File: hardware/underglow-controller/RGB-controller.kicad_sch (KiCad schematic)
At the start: 0 parts

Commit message: iasdf
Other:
- removed sheet Motor-Control
- removed sheet Pico Remote Proc
- note removed: "SPID = MOSI = RPRX SPIQ = MISO = RPTX"

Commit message: schematic rework progress
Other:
- sheet Connectors ports: added CAN_H, CAN_L, DI_1, DI_2, DI_3, DI_4, IGNITION_IN, PIXEL_1, PIXEL_2, RGB1_12V, RGB1_B, RGB1_G, RGB1_R, RGB2_12V, RGB2_B, RGB2_G, RGB2_R, USB_D_N, USB_D_P, USB_GND, USB_VBUS, VBAT; removed CAN_N, CAN_P, CONN_ESP_USB_D_N, CONN_ESP_USB_D_P, CONN_RP_USB_D_N, CONN_RP_USB_D_P, FUSE_OUT, GPI1, GPI2, GPI3, GPI4, GPO1, GPO2, GPO3, LEDA_OUT, MOTOR1_OUT1, MOTOR1_OUT2, MOTOR2_OUT1, MOTOR2_OUT2, VIN, VOUT
- sheet External-IO ports: added CSN, GP05, GP06, GPIO_GP05, GPIO_GP06, GPO4, IGNITION, LED1_IN, LED1_OUT, LED2_IN, LED2_OUT, LHI, MISO, MOSI, PWMI1, PWMI2, RGB1_12V, SCLK, VBATT, VIN; removed LEDA_IN, LEDA_OUT, VOUT_EN

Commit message: schematic almost done
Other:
- sheet SX1276 renamed SX1231
- sheet Connectors ports: added IGNITION, VBATT; removed IGNITION_IN, VBAT
- sheet ESP32-S3 ports: added DI_1, DI_2, DI_3, DI_4, LHI, PIXEL1_OUT, PIXEL2_OUT, RGB1_B, RGB1_G, RGB1_PWM, RGB1_R, RGB2_B, RGB2_G, RGB2_PWM, RGB2_R; removed FSPICS2, MCPWM0_ENA, MCPWM0_ENB, MCPWM0_INA, MCPWM0_INB, MCPWM1_ENA, MCPWM1_ENB, MCPWM1_INA, MCPWM1_INB, MCPWM_FAULT, MCPWM_RESET, MCPWM_SLEEP, RP2040_EN
- sheet External-IO ports: added DI_1, DI_2, DI_3, DI_4, PIXEL1_IN, PIXEL1_OUT, PIXEL2_IN, PIXEL2_OUT, RGB1_B, RGB1_G, RGB1_R, RGB2_12V, RGB2_B, RGB2_G, RGB2_R, TTL_DI_1, TTL_DI_2, TTL_DI_3, TTL_DI_4, TTL_RGB1_B, TTL_RGB1_G, TTL_RGB1_R, TTL_RGB2_B, TTL_RGB2_G, TTL_RGB2_R; removed GP01, GP02, GP03, GP05, GP06, GPI1, GPI2, GPI3, GPI4, GPIO_GP01, GPIO_GP02, GPIO_GP03, GPIO_GP04, GPIO_GP05, GPIO_GP06, GPIO_GPI1, GPIO_GPI2, GPIO_GPI3, GPIO_GPI4, GPO4, LED1_IN, LED1_OUT, LED2_IN, LED2_OUT
- sheet Power ports: added IGNITION, VBATT; removed VBAT, VIN, VOUT, VOUT_EN
- sheet SX1231: file SX1276.kicad_sch -> SX1231.kicad_sch

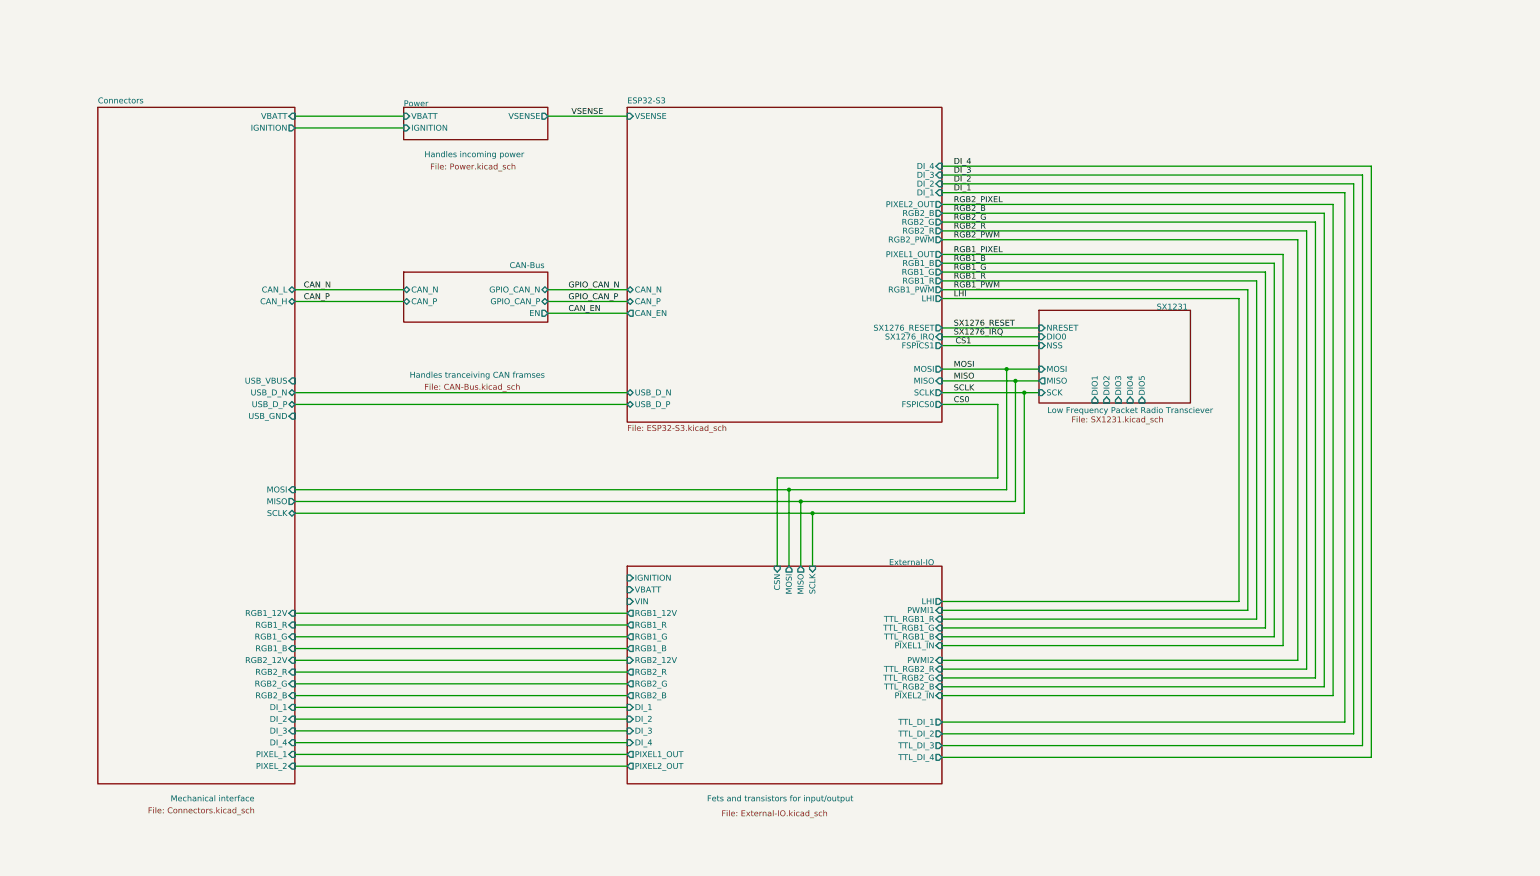
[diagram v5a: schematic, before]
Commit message: fix main sheet grid
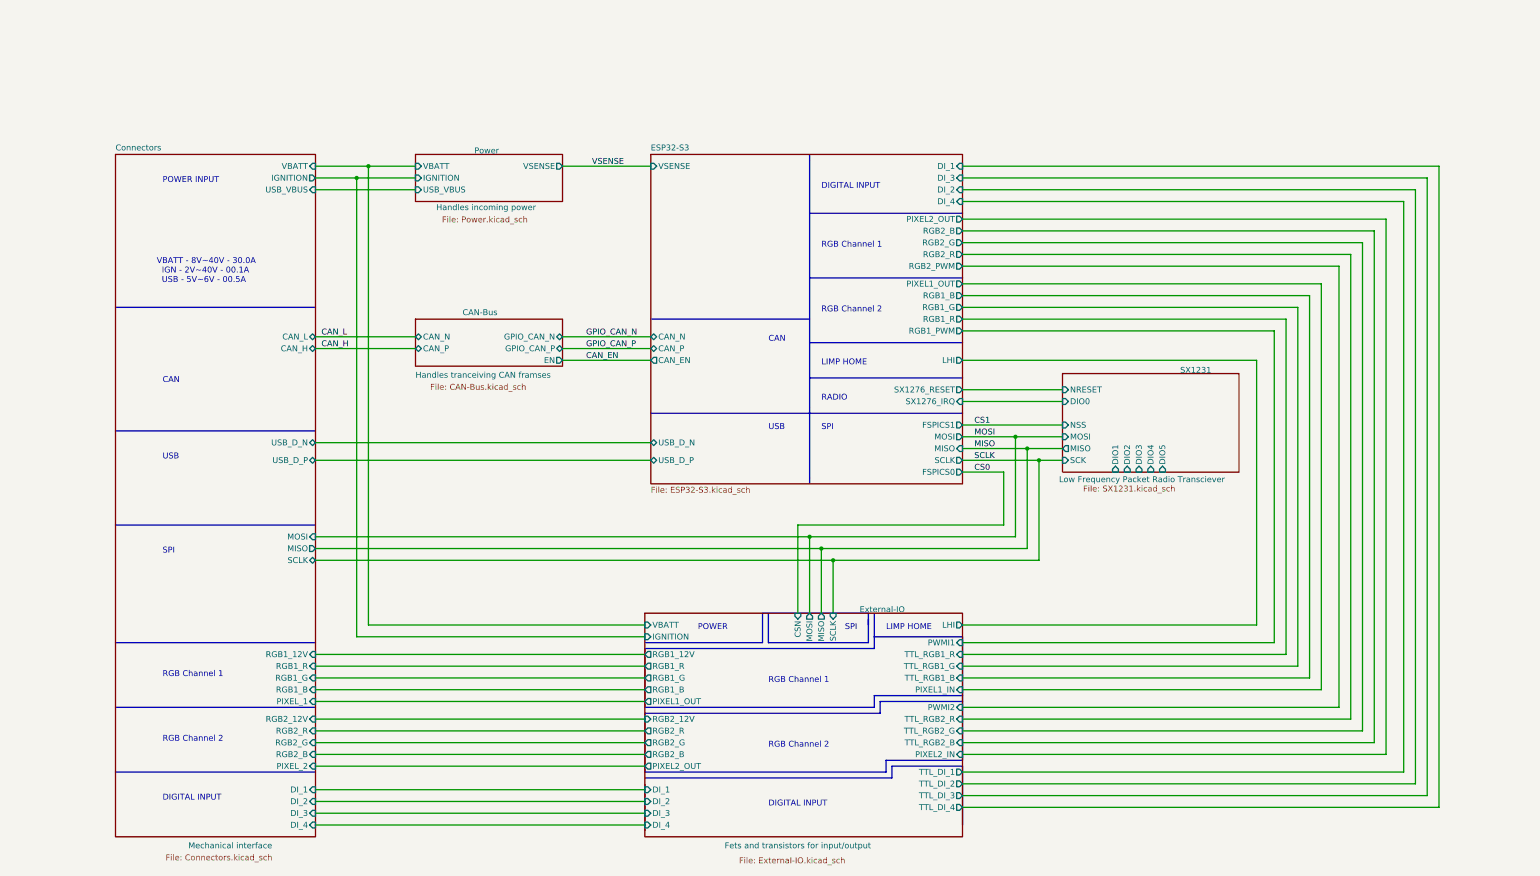
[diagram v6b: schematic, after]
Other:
- sheet Connectors ports: added none; removed USB_GND
- sheet External-IO ports: added none; removed VIN
- sheet Power ports: added USB_VBUS; removed none
- note added: "CAN"
- note added: "DIGITAL INPUT"
- note added: "LIMP HOME"
- note added: "POWER"
- note added: "POWER INPUT"
- note added: "RADIO"
- note added: "RGB Channel 1"
- note added: "RGB Channel 2"
- note added: "SPI"
- note added: "USB"
- note added: "VBATT - 8V~40V - 30.0A IGN - 2V~40V - 00.1A USB - 5V~6V - 00.5A"
